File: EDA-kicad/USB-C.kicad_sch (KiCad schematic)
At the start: 9 parts, among them J1 USBC-4-0-CX90MW9-24P1, U14 MUX HD3SS460RHRR, U15 USB SWITCH 2CHANNEL TS3USB221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

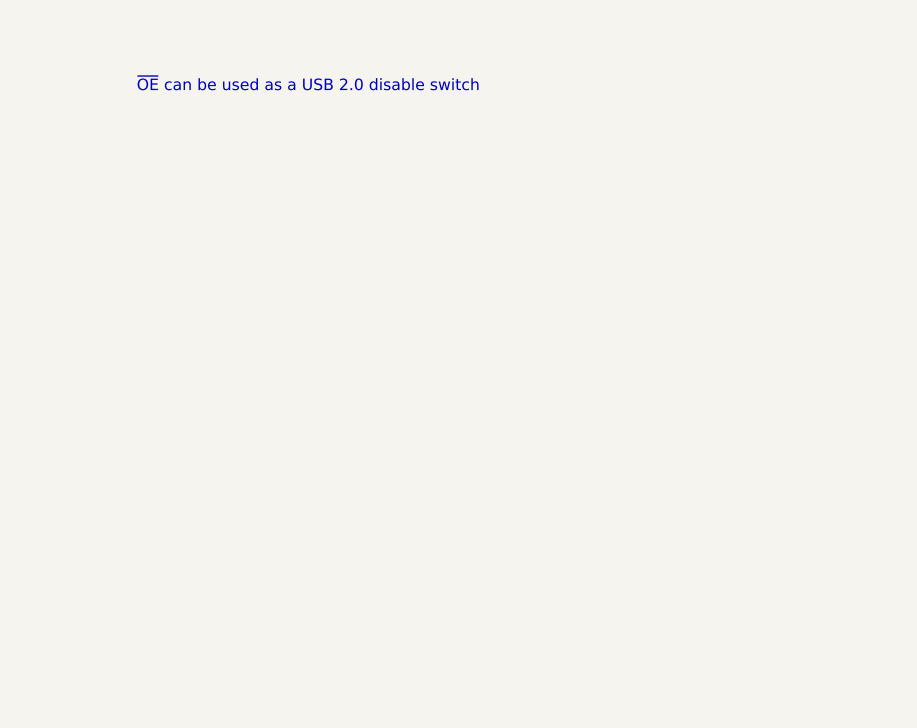
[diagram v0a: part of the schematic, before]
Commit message: added polarity detection
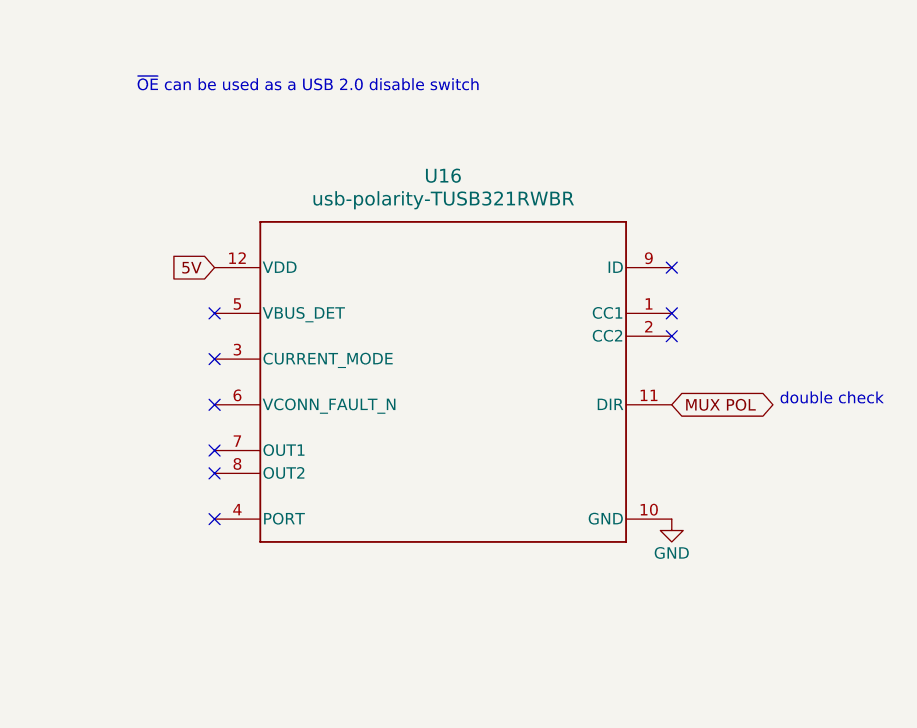
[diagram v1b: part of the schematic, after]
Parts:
- added U16: usb-polarity-TUSB321RWBR, SPIRIT-footprints:polarity-usb-TUSB321RWBR, symbol SPIRIT-components:usb-polarity-TUSB321RWBR
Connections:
- net GND: now also U16.10 (GND)
- net MUX POL: now also U16.11 (DIR)
- new net 5V: U16.12 (VDD)
- no-connect marks 14 -> 23
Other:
- note added: "double check"
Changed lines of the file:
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@@
 		)
 	)
+	(text "double check"
+		(exclude_from_sim no)
+		(at 274.32 146.812 0)
+		(effects
+			(font
+				(size 1.27 1.27)
+			)
+		)
+	)
 	(text "driven based on \"power good\"\nregister from BQ25792 (?)"
 		(exclude_from_sim no)
@@
 	)
 	(no_connect
+		(at 256.54 132.08)
+	)
+	(no_connect
+		(at 205.74 154.94)
+	)
+	(no_connect
 		(at 153.67 133.35)
 	)
 	(no_connect
+		(at 205.74 160.02)
+	)
+	(no_connect
 		(at 153.67 156.21)
 	)
@@
 	)
 	(no_connect
+		(at 205.74 147.32)
+	)
+	(no_connect
+		(at 205.74 152.4)
+	)
+	(no_connect
+		(at 205.74 142.24)
+	)
+	(no_connect
+		(at 256.54 137.16)
+	)
+	(no_connect
 		(at 153.67 135.89)
 	)
@@
 	)
 	(no_connect
+		(at 256.54 139.7)
+	)
+	(no_connect
 		(at 153.67 158.75)
 	)
@@
 	)
 	(no_connect
+		(at 205.74 137.16)
+	)
+	(no_connect
 		(at 113.03 181.61)
 	)
@@
 		)
 	)
+	(global_label "5V"
+		(shape input)
+		(at 205.74 132.08 180)
+		(fields_autoplaced yes)
+		(effects
+			(font
+				(size 1.27 1.27)
+			)
+			(justify right)
+		)
+		(property "Intersheetrefs" "${INTERSHEET_REFS}"
+			(at 200.4567 132.08 0)
+			(effects
+				(font
+					(size 1.27 1.27)
+				)
+				(justify right)
+				(hide yes)
+			)
+		)
+	)
 	(global_label "RX1-"
 		(shape bidirectional)
@@
 		)
 	)
+	(global_label "MUX POL"
+		(shape bidirectional)
+		(at 256.54 147.32 0)
+		(fields_autoplaced yes)
+		(effects
+			(font
+				(size 1.27 1.27)
+			)
+			(justify left)
+		)
+		(property "Intersheetrefs" "${INTERSHEET_REFS}"
+			(at 269.2241 147.32 0)
+			(effects
+				(font
+					(size 1.27 1.27)
+				)
+				(justify left)
+				(hide yes)
+			)
+		)
+	)
 	(global_label "D+"
 		(shape bidirectional)
@@
 	)
 	(symbol
+		(lib_name "GND_3")
+		(lib_id "power:GND")
+		(at 256.54 160.02 0)
+		(unit 1)
+		(exclude_from_sim no)
+		(in_bom yes)
+		(on_board yes)
+		(dnp no)
+		(property "Reference" "#PWR0153"
+			(at 256.54 166.37 0)
+			(effects
+				(font
+					(size 1.27 1.27)
+				)
+				(hide yes)
+			)
+		)
+		(property "Value" "GND"
+			(at 256.54 163.83 0)
+			(effects
+				(font
+					(size 1.27 1.27)
+				)
+			)
+		)
+		(property "Footprint" ""
+			(at 256.54 160.02 0)
+			(effects
+				(font
+					(size 1.27 1.27)
+				)
+				(hide yes)
+			)
+		)
+		(property "Datasheet" ""
+			(at 256.54 160.02 0)
+			(effects
+				(font
+					(size 1.27 1.27)
+				)
+				(hide yes)
+			)
+		)
+		(property "Description" ""
+			(at 256.54 160.02 0)
+			(effects
+				(font
+					(size 1.27 1.27)
+				)
+				(hide yes)
+			)
+		)
+		(pin "1"
+		)
+		(instances
+			(project "cm5-carrier"
+				(path "/28c5e4fe-1ec7-4477-97f0-d2ec1401fad5/4d20c3c8-7f3b-4711-a43f-15c2a08af985"
+					(reference "#PWR0153")
+					(unit 1)
+				)
+			)
+		)
+	)
+	(symbol
 		(lib_id "SPIRIT-components:USB-protection-diode-PESD5V0C1USFYL")
 		(at 26.67 48.26 0)
@@
 					(unit 1)
 				)
+			)
+		)
+	)
+	(symbol
+		(lib_id "SPIRIT-components:usb-polarity-TUSB321RWBR")
+		(at 231.14 144.78 0)
+		(unit 1)
+		(exclude_from_sim no)
+		(in_bom yes)
+		(on_board yes)
+		(dnp no)
+		(fields_autoplaced yes)
+		(property "Reference" "U16"
+			(at 231.14 121.92 0)
+			(effects
+				(font
+					(size 1.524 1.524)
+				)
+			)
+		)
+		(property "Value" "usb-polarity-TUSB321RWBR"
+			(at 231.14 124.46 0)
+			(effects
+				(font
+					(size 1.524 1.524)
+				)
+			)
+		)
+		(property "Footprint" "SPIRIT-footprints:polarity-usb-TUSB321RWBR"
+			(at 231.14 144.78 0)
+			(effects
+				(font
+					(size 1.27 1.27)
+					(italic yes)
+				)
+				(hide yes)
+			)
+		)
+		(property "Datasheet" "https://www.ti.com/lit/gpn/tusb321"
+			(at 231.14 144.78 0)
+			(effects
+				(font
+					(size 1.27 1.27)
+					(italic yes)
+				)
+				(hide yes)
+			)
+		)
+		(property "Description" ""
+			(at 231.14 144.78 0)
+			(effects
+				(font
+					(size 1.27 1.27)
+				)
+				(hide yes)
+			)
+		)
+		(pin "9"
+		)
+		(pin "10"
+		)
+		(pin "11"
+		)
+		(pin "1"
+		)
+		(pin "8"
+		)
+		(pin "6"
+		)
+		(pin "7"
+		)
+		(pin "5"
+		)
+		(pin "12"
+		)
+		(pin "3"
+		)
+		(pin "2"
+		)
+		(pin "4"
+		)
+		(instances
+			(project "cm5-carrier"
+				(path "/28c5e4fe-1ec7-4477-97f0-d2ec1401fad5/4d20c3c8-7f3b-4711-a43f-15c2a08af985"
+					(reference "U16")
+					(unit 1)
+				)
